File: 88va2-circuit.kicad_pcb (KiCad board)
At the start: 4 copper layers, 380 x 237.5 mm, 52 parts, among them CN2 FDD, CN4 TEXT BUS, CN5 LED, IC1 D65101GD055, IC13 SN74ALS374N, IC20 7407, IC21 uPD4990AC, IC22 DIP-14_W7.62mm, IC65 D65101GD110, IC8 SN74ALS374N, IC9 D65200GD076, X2 32.768K

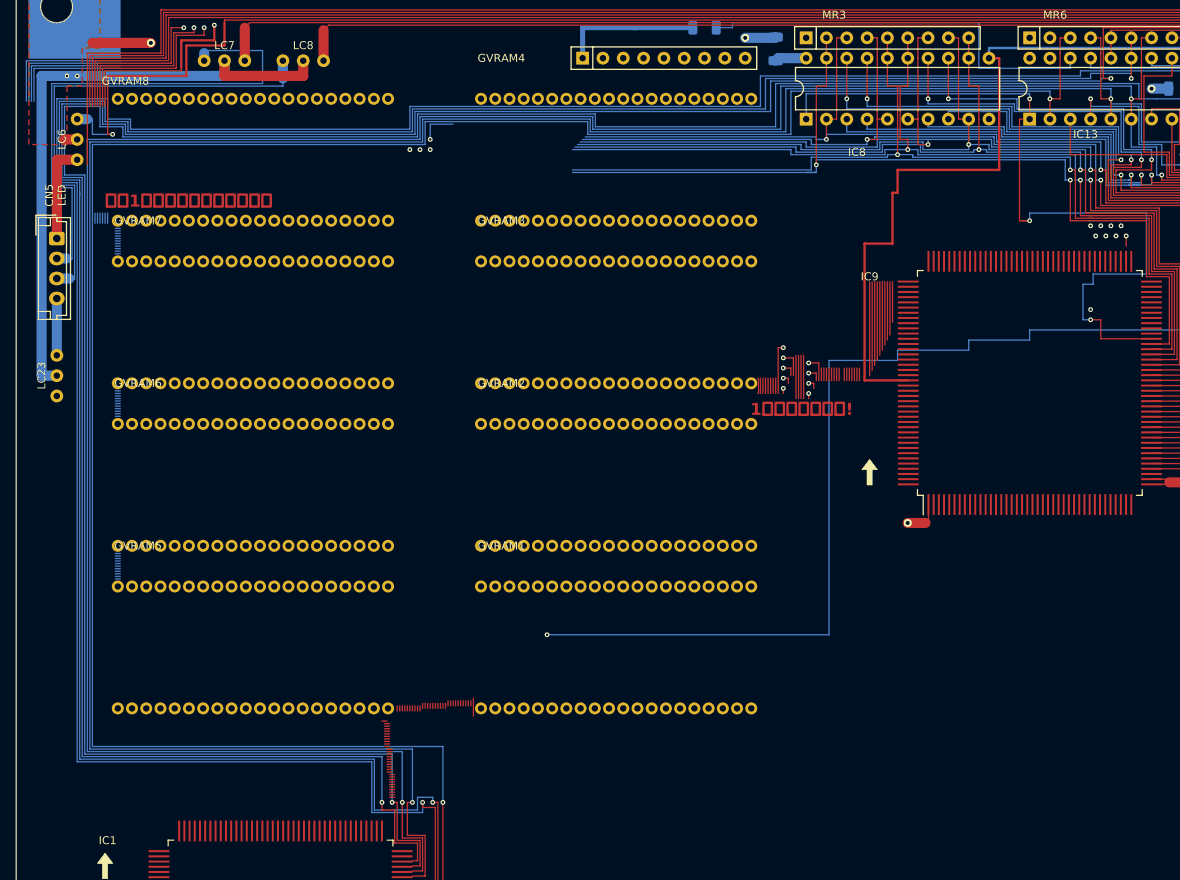
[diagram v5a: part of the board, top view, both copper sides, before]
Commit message: fix GVRAM footprints and position
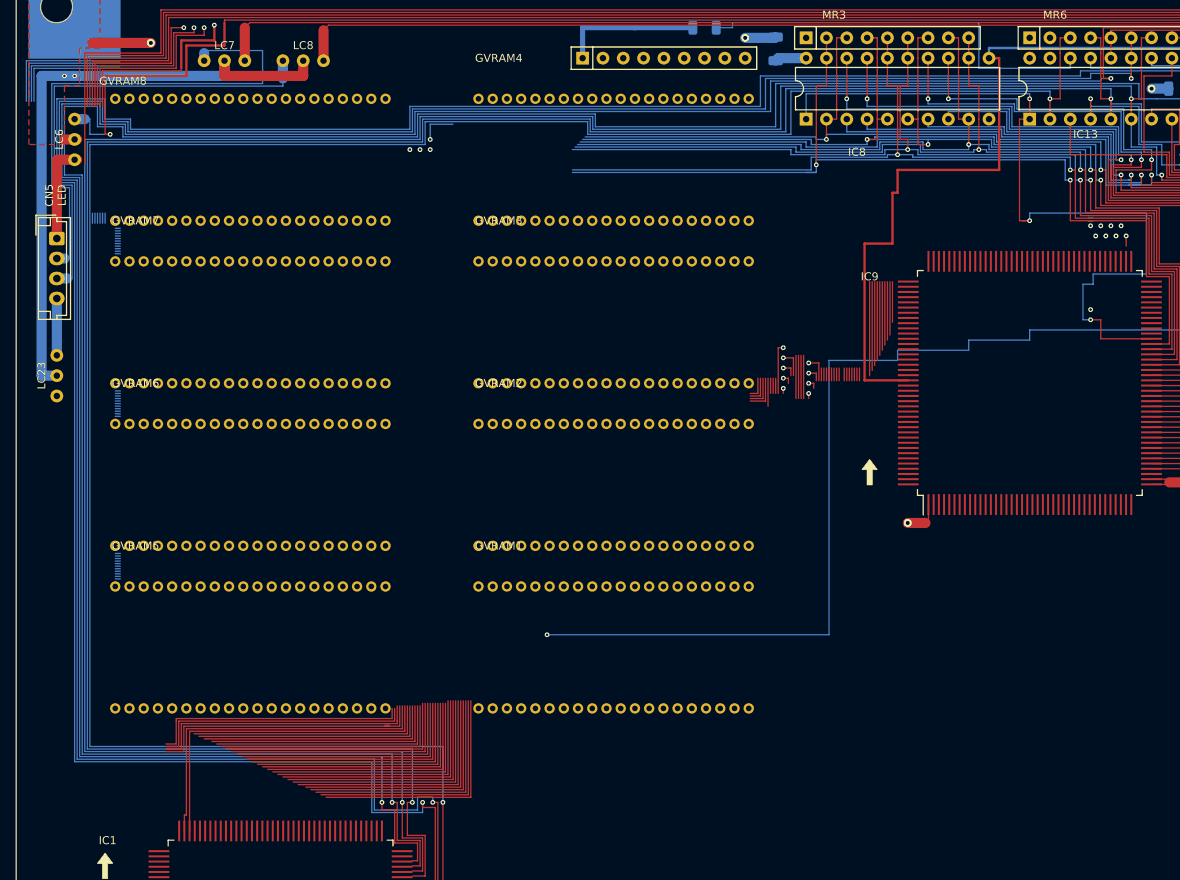
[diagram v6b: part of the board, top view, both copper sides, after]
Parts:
- moved LC6 0.32 mm to (20.0, 40.6)
- moved GVRAM5 0.32 mm to (25.0, 109.2)
- moved GVRAM6 0.32 mm to (25.0, 88.9)
- moved GVRAM7 0.32 mm to (25.0, 68.6)
- moved GVRAM8 0.32 mm to (25.0, 48.2)
- moved GVRAM1 0.32 mm to (70.4, 109.2)
- moved GVRAM2 0.32 mm to (70.4, 88.9)
- moved GVRAM3 0.32 mm to (70.4, 68.6)
- moved GVRAM4 0.32 mm to (70.4, 48.2)
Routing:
- net (no net): track 1961.9 -> 2939.4 mm
- net Net-(CN5-Pin_3): track 60.0 -> 58.7 mm
- net Net-(CN5-Pin_2): track 65.2 -> 63.9 mm
- net GCS0: track 356.4 -> 357.1 mm
- net GCS1: track 344.9 -> 345.5 mm
- net DTM0: track 285.1 -> 285.8 mm
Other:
- board text removed: "1ライン入らない!"
- board text removed: "もう1グリッド左に寄せたい！"

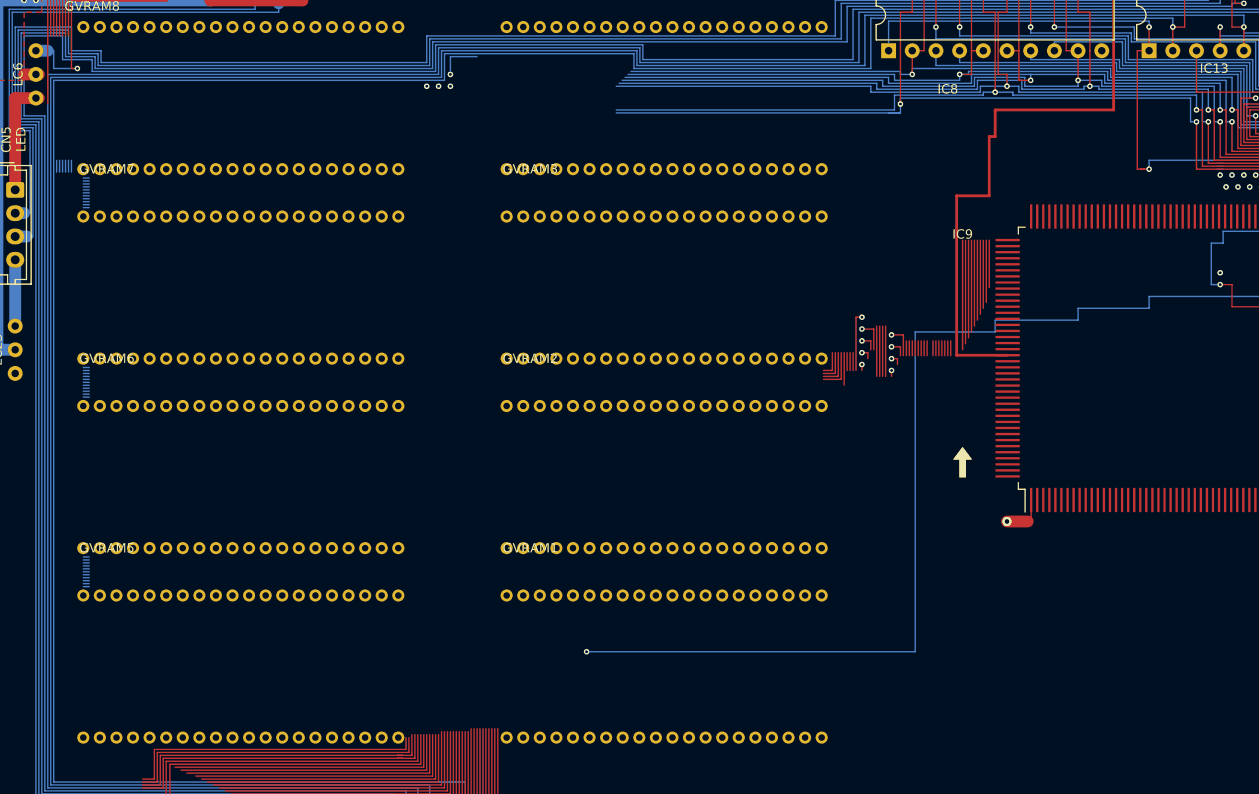
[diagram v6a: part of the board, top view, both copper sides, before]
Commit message: wire GVRAM SCLKx
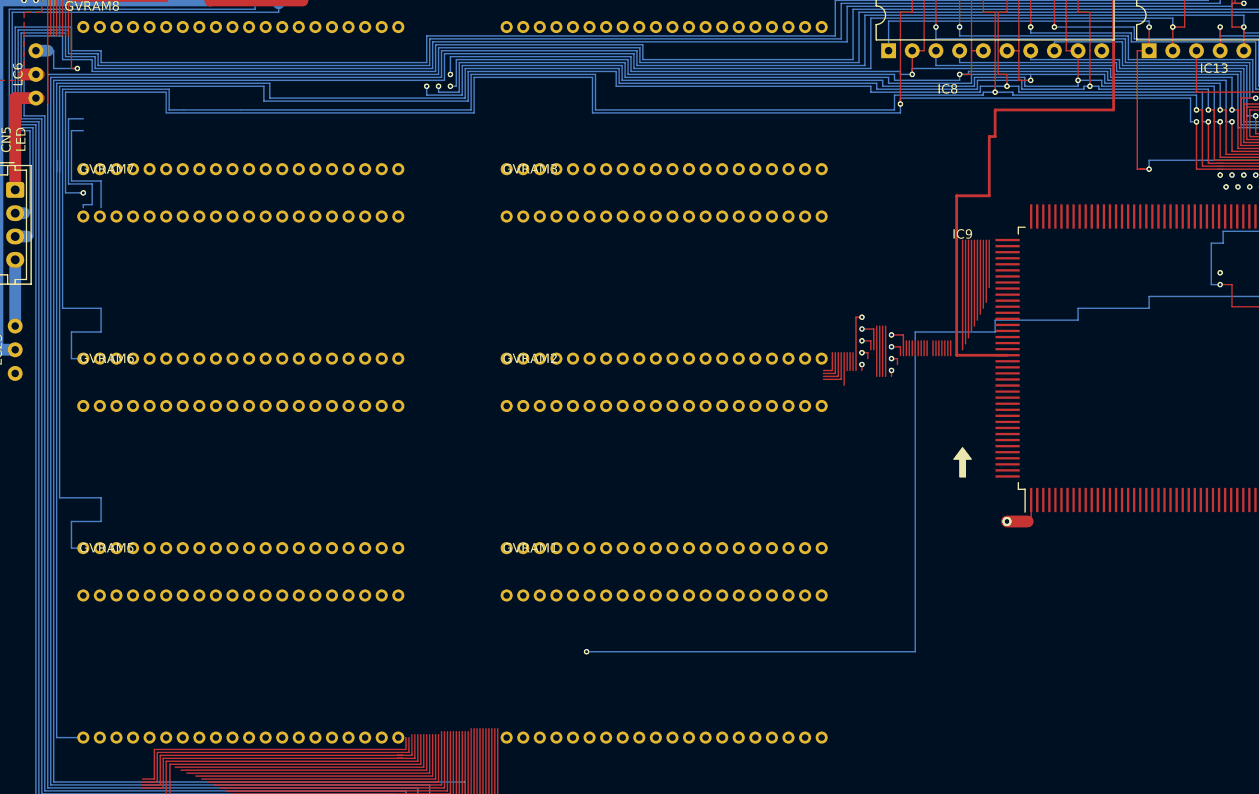
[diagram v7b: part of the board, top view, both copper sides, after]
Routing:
- net SCLK4: track 122.8 -> 263.8 mm
- net SCLK5: track 120.9 -> 246.6 mm
- net SCLK6: track 119.6 -> 226.3 mm
- net SCLK7: track 119.9 -> 200.5 mm, vias 2 -> 3
- net SCLK3: track 125.3 -> 152.0 mm, vias 2 -> 3
- net SCLK2: track 127.3 -> 152.7 mm, vias 2 -> 3
- net SCLK1: track 127.3 -> 150.8 mm, vias 2 -> 3
- net SCLK0: track 126.7 -> 149.5 mm, vias 2 -> 3
- net (no net): track 2939.4 -> 2933.4 mm, vias 51 -> 47

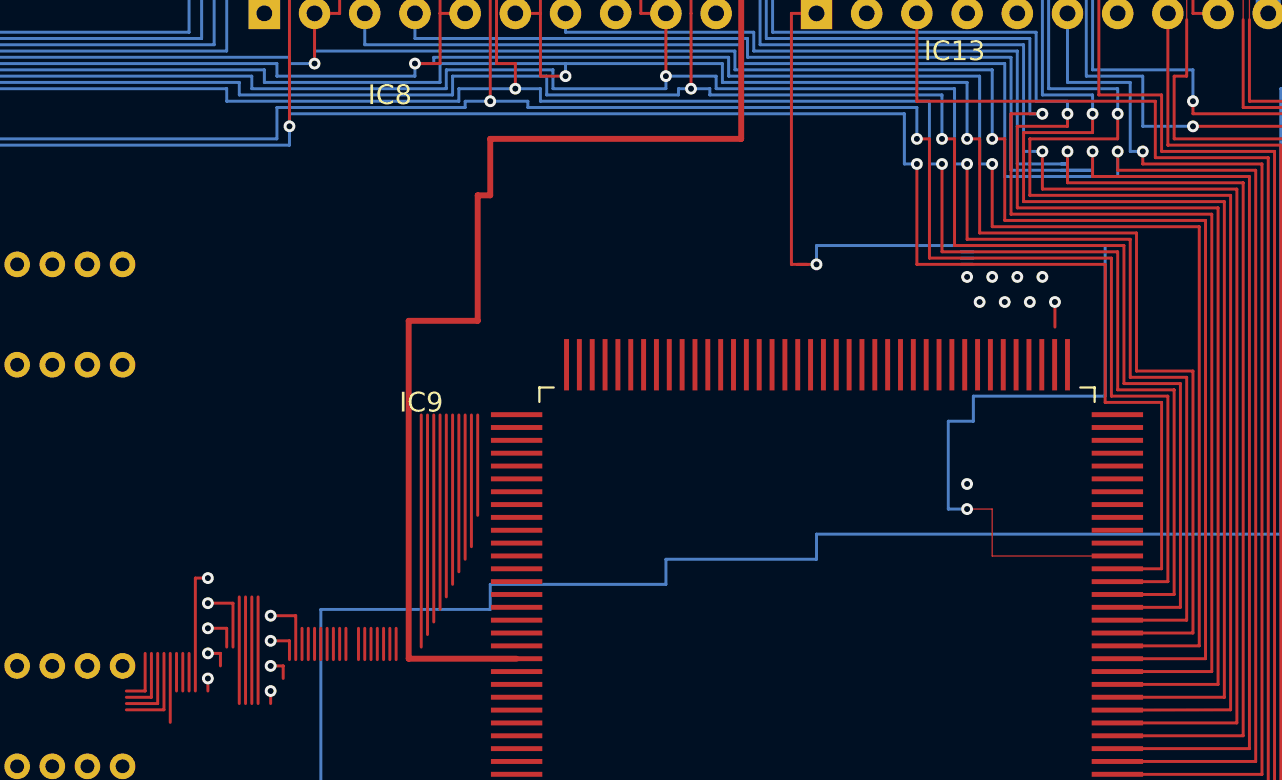
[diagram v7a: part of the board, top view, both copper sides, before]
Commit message: wiring IC9
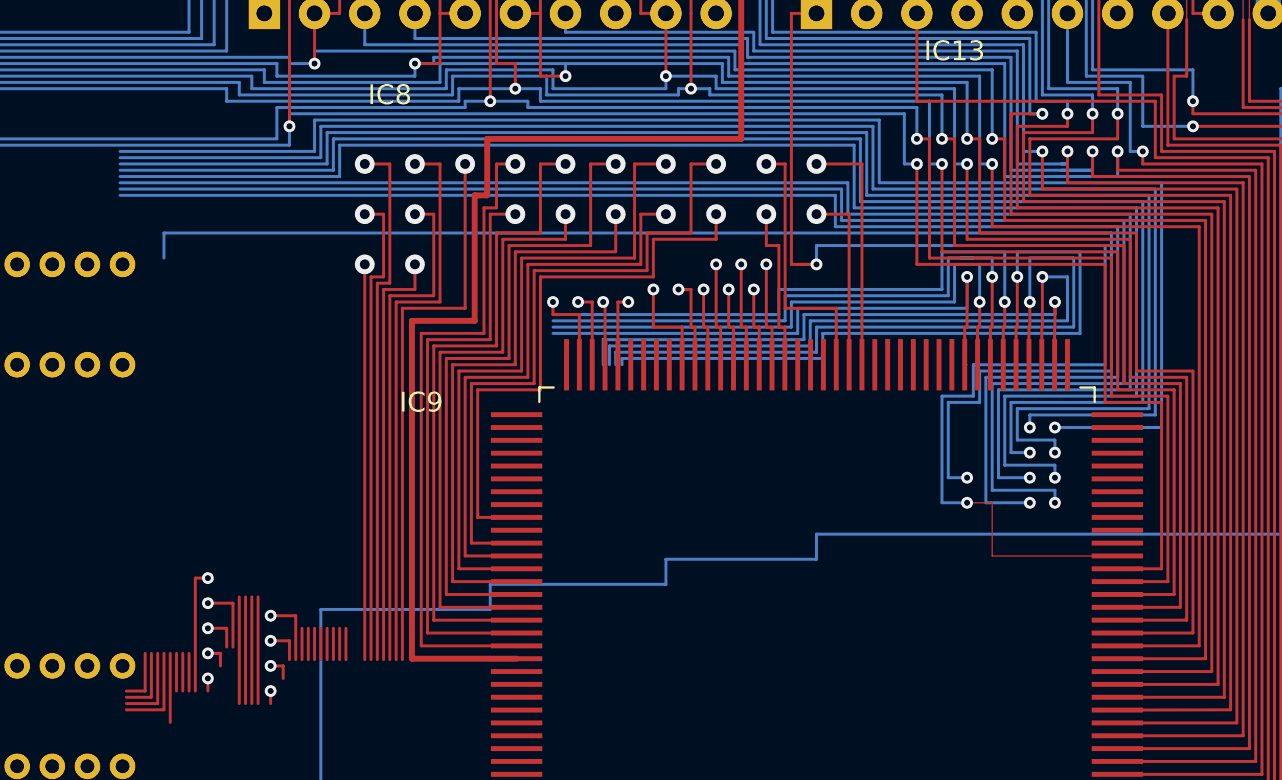
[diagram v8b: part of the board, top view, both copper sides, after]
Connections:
- IC9 pad 103: (no net) -> unconnected-(IC9-Pad103)
- IC9 pad 129: (no net) -> unconnected-(IC9-Pad129)
- IC9 pad 131: (no net) -> unconnected-(IC9-Pad131)
- IC9 pad 132: (no net) -> unconnected-(IC9-Pad132)
- IC9 pad 133: (no net) -> unconnected-(IC9-Pad133)
- IC9 pad 134: (no net) -> unconnected-(IC9-Pad134)
- IC9 pad 135: (no net) -> unconnected-(IC9-Pad135)
- IC9 pad 136: (no net) -> unconnected-(IC9-Pad136)
- IC9 pad 137: (no net) -> unconnected-(IC9-Pad137)
- IC9 pad 138: (no net) -> unconnected-(IC9-Pad138)
- IC9 pad 139: (no net) -> unconnected-(IC9-Pad139)
- IC9 pad 142: (no net) -> unconnected-(IC9-Pad142)
- IC9 pad 143: (no net) -> unconnected-(IC9-Pad143)
- IC9 pad 144: (no net) -> unconnected-(IC9-Pad144)
- IC9 pad 145: (no net) -> unconnected-(IC9-Pad145)
- IC9 pad 146: (no net) -> unconnected-(IC9-Pad146)
- IC9 pad 147: (no net) -> unconnected-(IC9-Pad147)
- IC9 pad 148: (no net) -> unconnected-(IC9-Pad148)
- IC9 pad 97: (no net) -> unconnected-(IC9-Pad97)
- IC9 pad 98: (no net) -> unconnected-(IC9-Pad98)
- IC9 pad 99: (no net) -> unconnected-(IC9-Pad99)
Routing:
- net (no net): track 2933.4 -> 4000.6 mm, vias 47 -> 74
- net unconnected-(IC9-Pad139): track 0.00 -> 34.0 mm, vias 0 -> 1
- net unconnected-(IC9-Pad137): track 0.00 -> 33.9 mm, vias 0 -> 1
- net unconnected-(IC9-Pad135): track 0.00 -> 33.9 mm, vias 0 -> 1
- net unconnected-(IC9-Pad133): track 0.00 -> 33.9 mm, vias 0 -> 1
- net unconnected-(IC9-Pad131): track 0.00 -> 33.9 mm, vias 0 -> 1
- net unconnected-(IC9-Pad138): track 0.00 -> 30.1 mm, vias 0 -> 1
- net unconnected-(IC9-Pad136): track 0.00 -> 30.1 mm, vias 0 -> 1
- net unconnected-(IC9-Pad134): track 0.00 -> 30.1 mm, vias 0 -> 1
- net unconnected-(IC9-Pad132): track 0.00 -> 30.1 mm, vias 0 -> 1
- net unconnected-(IC9-Pad129): track 0.00 -> 29.4 mm, vias 0 -> 1
- net unconnected-(IC9-Pad99): track 0.00 -> 13.7 mm, vias 0 -> 1
- net unconnected-(IC9-Pad97): track 0.00 -> 12.5 mm, vias 0 -> 1
- net unconnected-(IC9-Pad98): track 0.00 -> 9.48 mm, vias 0 -> 1
- net unconnected-(IC9-Pad103): track 0.00 -> 8.56 mm, vias 0 -> 1
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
